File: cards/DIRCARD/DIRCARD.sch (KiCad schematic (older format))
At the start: 40 parts, among them J101 BICK, J102 SDTO, J103 LRCK, J104 MCLK, J105 OPTICAL IN, J106 COAX_IN, J107 PCIe x4 Slot, SW101 SW_DIP_x02, U101 AK4118, U102 BA033CC0T

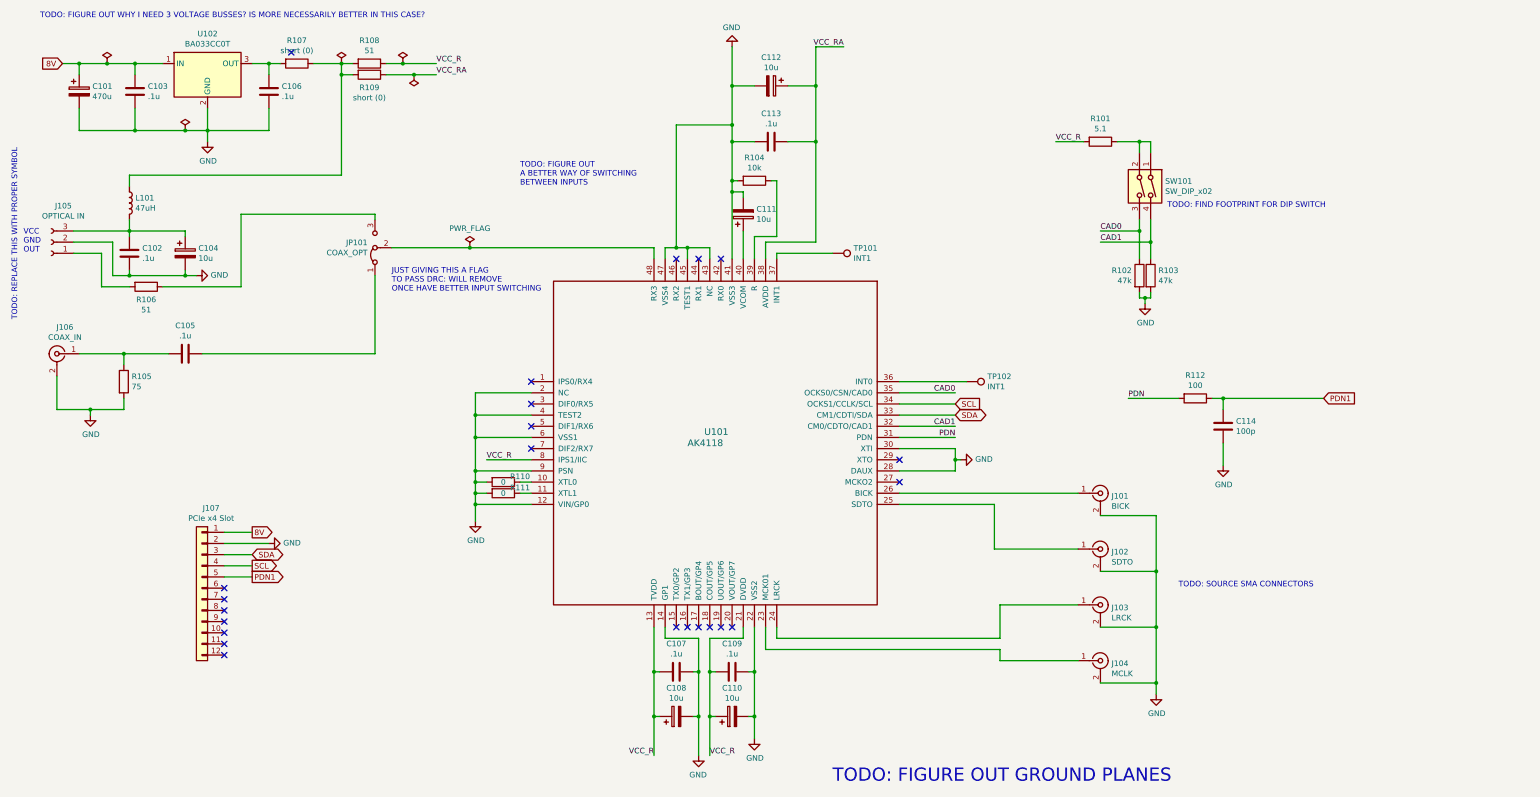
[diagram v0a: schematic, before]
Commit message: Add source termination to critical transmission lines, as well as a note about LVMCMOS vs LVDS brought up by chris719
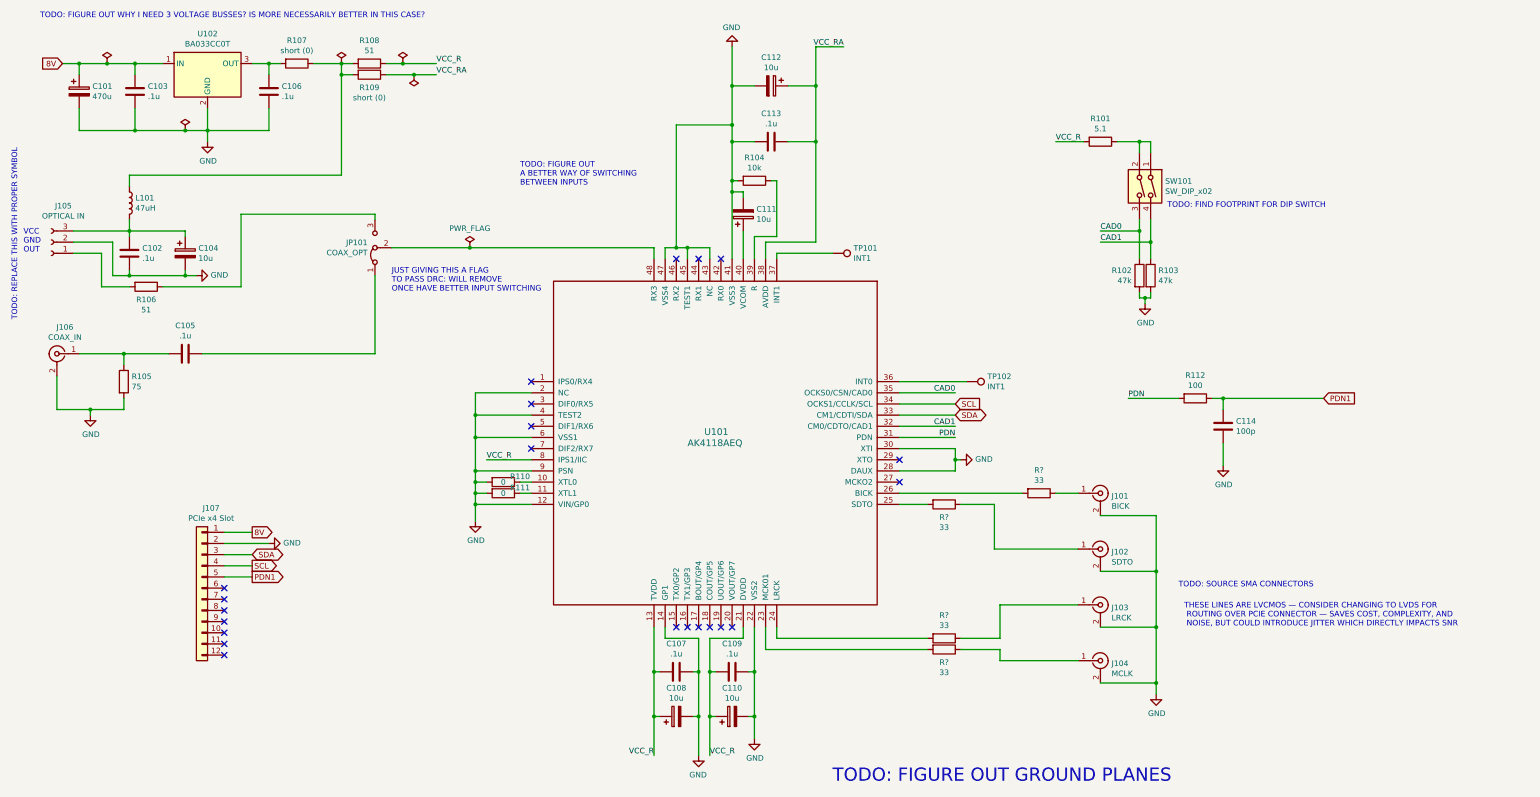
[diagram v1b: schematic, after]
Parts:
- added R? (x4): 33, symbol Device:R
- U101: value AK4118 -> AK4118AEQ
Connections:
- net at J104.1 (In): now also R?.1; no longer U101.23 (MCK01)
- net at J103.1 (In): now also R?.1; no longer U101.24 (LRCK)
- net at J102.1 (In): now also R?.1; no longer U101.25 (SDTO)
- net at J101.1 (In): now also R?.1; no longer U101.26 (BICK)
- new net: R?.2, U101.23 (MCK01)
- new net: R?.2, U101.24 (LRCK)
- new net: R?.2, U101.26 (BICK)
- new net: R?.2, U101.25 (SDTO)
- no-connect marks 23 -> 22
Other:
- note added: "THESE LINES ARE LVCMOS — CONSIDER CHANGING TO LVDS FOR\n ROUTING OVER PCIE CONNECTOR — SAVES COST, COMPLEXITY, AND\n NOISE, BUT COULD INTRODUCE JITTER WHICH DIRECTLY IMPACTS SNR"
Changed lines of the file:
@@
 	10150 6800 10850 6800
 Wire Wire Line
-	8050 6700 10150 6700
+	8050 6700 9500 6700
 Wire Wire Line
 	10150 6600 10150 6300
@@
 	10150 6300 10850 6300
 Wire Wire Line
-	8150 6600 10150 6600
+	8150 6600 9500 6600
 Wire Wire Line
 	10100 5400 10100 5800
@@
 	10100 5800 10850 5800
 Wire Wire Line
-	9250 5400 10100 5400
-Wire Wire Line
-	9250 5300 10850 5300
+	9250 5400 9500 5400
 Wire Wire Line
 	11050 5500 11550 5500
@@
 P 8150 3200
 F 0 "U101" V 9700 2550 60  0000 L CNN
-F 1 "AK4118" V 9800 2400 60  0000 L CNN
+F 1 "AK4118AEQ" V 9800 2400 60  0000 L CNN
 F 2 "Package_QFP:LQFP-48_7x7mm_P0.5mm" H 8300 3250 60  0001 R CNN
 F 3 "" H 8300 3050 60  0001 R CNN
@@
 NoConn ~ 3200 6650
 NoConn ~ 3200 6750
-NoConn ~ 3800 1350
 $Comp
 L power:PWR_FLAG #FLG0106
@@
 Text Notes 4700 3500 0    50   ~ 0
 JUST GIVING THIS A FLAG\nTO PASS DRC: WILL REMOVE \nONCE HAVE BETTER INPUT SWITCHING
+Text Notes 11800 6500 0    50   ~ 0
+THESE LINES ARE LVCMOS — CONSIDER CHANGING TO LVDS FOR\n ROUTING OVER PCIE CONNECTOR — SAVES COST, COMPLEXITY, AND\n NOISE, BUT COULD INTRODUCE JITTER WHICH DIRECTLY IMPACTS SNR
+$Comp
+L Device:R R?
+U 1 1 5E12E763
+P 9650 6700
+F 0 "R?" V 9765 6700 50  0000 C CNN
+F 1 "33" V 9856 6700 50  0000 C CNN
+F 2 "" V 9580 6700 50  0001 C CNN
+F 3 "~" H 9650 6700 50  0001 C CNN
+	1    9650 6700
+	0    1    1    0
+$EndComp
+Wire Wire Line
+	9800 6700 10150 6700
+$Comp
+L Device:R R?
+U 1 1 5E12EE66
+P 9650 6600
+F 0 "R?" V 9443 6600 50  0000 C CNN
+F 1 "33" V 9534 6600 50  0000 C CNN
+F 2 "" V 9580 6600 50  0001 C CNN
+F 3 "~" H 9650 6600 50  0001 C CNN
+	1    9650 6600
+	0    1    1    0
+$EndComp
+Wire Wire Line
+	9800 6600 10150 6600
+$Comp
+L Device:R R?
+U 1 1 5E12F308
+P 10500 5300
+F 0 "R?" V 10293 5300 50  0000 C CNN
+F 1 "33" V 10384 5300 50  0000 C CNN
+F 2 "" V 10430 5300 50  0001 C CNN
+F 3 "~" H 10500 5300 50  0001 C CNN
+	1    10500 5300
+	0    1    1    0
+$EndComp
+$Comp
+L Device:R R?
+U 1 1 5E12FA5C
+P 9650 5400
+F 0 "R?" V 9765 5400 50  0000 C CNN
+F 1 "33" V 9856 5400 50  0000 C CNN
+F 2 "" V 9580 5400 50  0001 C CNN
+F 3 "~" H 9650 5400 50  0001 C CNN
+	1    9650 5400
+	0    1    1    0
+$EndComp
+Wire Wire Line
+	9800 5400 10100 5400
+Wire Wire Line
+	10650 5300 10850 5300
+Wire Wire Line
+	9250 5300 10350 5300
 $EndSCHEMATC

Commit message: Split ground plane
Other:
- note added: "ANALOG GROUND"
- note added: "DIGITAL GROUND"
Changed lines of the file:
@@
 	7950 3000 7950 3200
-Wire Wire Line
-	8650 3150 8150 3150
 Wire Wire Line
 	8150 3150 8150 3200
@@
 Wire Wire Line
 	9250 5300 10350 5300
+Wire Notes Line
+	6150 4950 8100 4950
+Wire Wire Line
+	8650 3150 8150 3150
+Wire Notes Line
+	8100 3400 8100 4950
+Text Notes 6900 4150 0    50   ~ 0
+ANALOG GROUND
+Text Notes 6900 5350 0    50   ~ 0
+DIGITAL GROUND
 $EndSCHEMATC
